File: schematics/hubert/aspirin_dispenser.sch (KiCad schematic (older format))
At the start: 3 parts, among them M6 NEMA 17 Stepper Motor

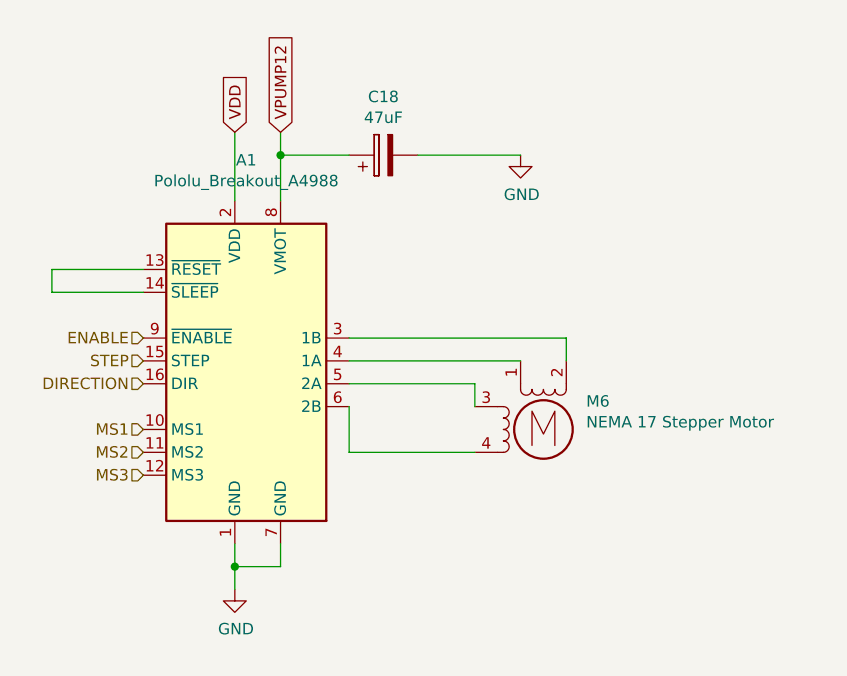
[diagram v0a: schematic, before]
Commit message: updated schematics
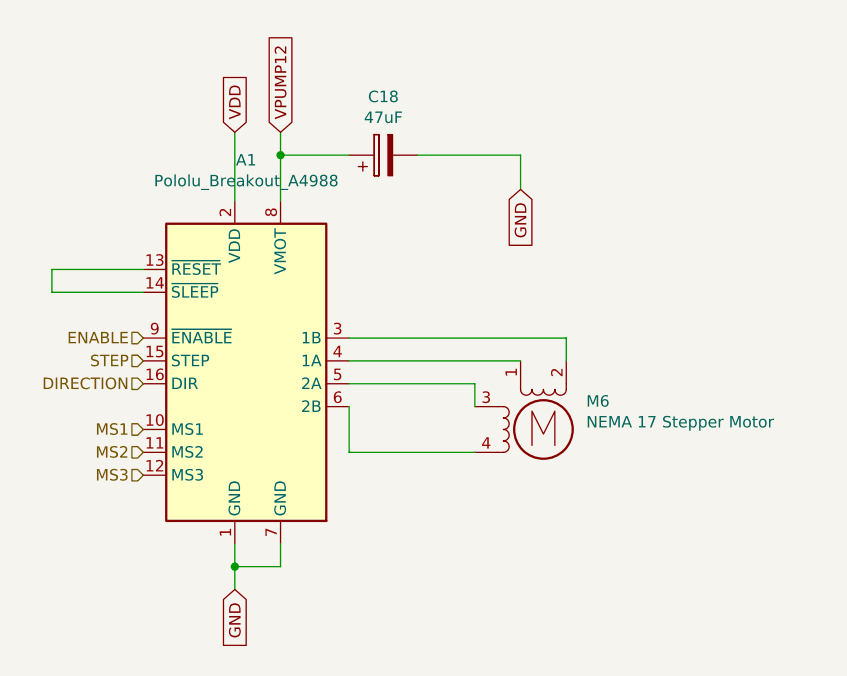
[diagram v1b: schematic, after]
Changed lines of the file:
@@
 $Descr A4 11693 8268
 encoding utf-8
-Sheet 5 6
-Title ""
-Date ""
-Rev ""
+Sheet 5 7
+Title "Hubert"
+Date "2018-11-02"
+Rev "1.1"
 Comp ""
 Comment1 ""
@@
 Wire Wire Line
 	4700 2950 5100 2950
-$Comp
-L power:GND #PWR015
-U 1 1 5BDB44B8
-P 5500 4250
-F 0 "#PWR015" H 5500 4000 50  0001 C CNN
-F 1 "GND" H 5505 4077 50  0000 C CNN
-F 2 "" H 5500 4250 50  0001 C CNN
-F 3 "" H 5500 4250 50  0001 C CNN
-	1    5500 4250
-	1    0    0    -1
-$EndComp
 Wire Wire Line
 	5500 4050 5500 4150
@@
 Wire Wire Line
 	5700 2350 5700 2250
-$Comp
-L power:GND #PWR017
-U 1 1 5BDB595D
-P 6750 2350
-F 0 "#PWR017" H 6750 2100 50  0001 C CNN
-F 1 "GND" H 6755 2177 50  0000 C CNN
-F 2 "" H 6750 2350 50  0001 C CNN
-F 3 "" H 6750 2350 50  0001 C CNN
-	1    6750 2350
-	1    0    0    -1
-$EndComp
 Wire Wire Line
 	6300 2350 6750 2350
@@
 Text GLabel 5700 2250 1    50   Input ~ 0
 VPUMP12
+Text GLabel 5500 4250 3    50   Input ~ 0
+GND
+Text GLabel 6750 2500 3    50   Input ~ 0
+GND
+Wire Wire Line
+	6750 2500 6750 2350
 $EndSCHEMATC

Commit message: fixed ERC problems and added connector for input pins
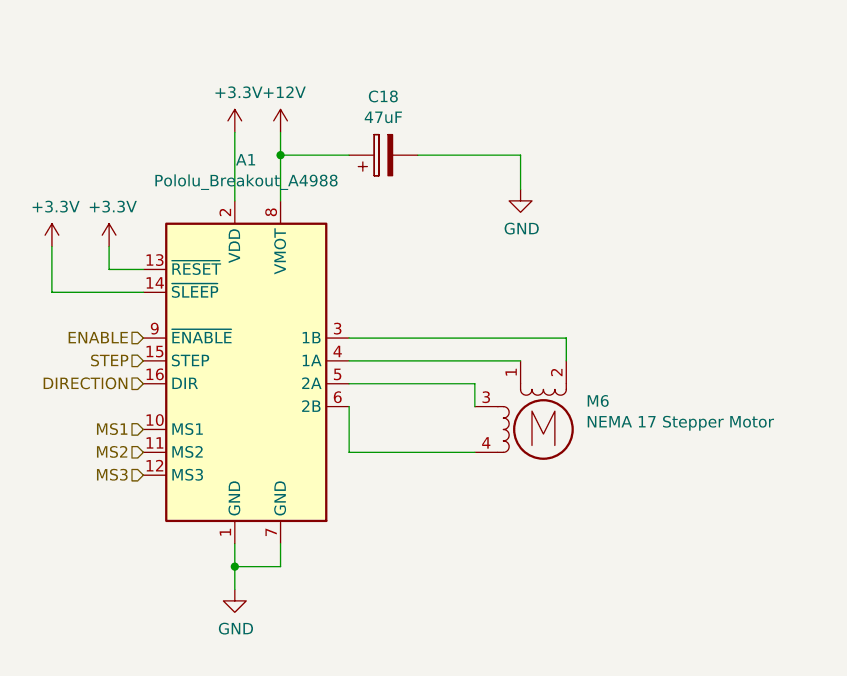
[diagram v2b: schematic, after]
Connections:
- net VDD is gone; now on net +3V3: A1.2 (VDD)
- net +3V3: now reaches A1.13 (~RESET), A1.14 (~SLEEP)
- net VPUMP12 renamed +12V
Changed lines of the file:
@@
 $EndComp
-Wire Wire Line
-	5100 2850 4700 2850
-Wire Wire Line
-	4700 2850 4700 2950
-Wire Wire Line
-	4700 2950 5100 2950
 Wire Wire Line
 	5500 4050 5500 4150
@@
 Wire Wire Line
 	5500 2250 5500 2550
-Text GLabel 5500 2250 1    50   Input ~ 0
-VDD
-Text GLabel 5700 2250 1    50   Input ~ 0
-VPUMP12
-Text GLabel 5500 4250 3    50   Input ~ 0
-GND
-Text GLabel 6750 2500 3    50   Input ~ 0
-GND
 Wire Wire Line
 	6750 2500 6750 2350
+$Comp
+L power:GND #PWR0121
+U 1 1 5BE2C7E5
+P 6750 2500
+F 0 "#PWR0121" H 6750 2250 50  0001 C CNN
+F 1 "GND" H 6755 2327 50  0000 C CNN
+F 2 "" H 6750 2500 50  0001 C CNN
+F 3 "" H 6750 2500 50  0001 C CNN
+	1    6750 2500
+	1    0    0    -1
+$EndComp
+$Comp
+L power:GND #PWR0122
+U 1 1 5BE2C7FD
+P 5500 4250
+F 0 "#PWR0122" H 5500 4000 50  0001 C CNN
+F 1 "GND" H 5505 4077 50  0000 C CNN
+F 2 "" H 5500 4250 50  0001 C CNN
+F 3 "" H 5500 4250 50  0001 C CNN
+	1    5500 4250
+	1    0    0    -1
+$EndComp
+$Comp
+L power:+12V #PWR0123
+U 1 1 5BE2C836
+P 5700 2250
+F 0 "#PWR0123" H 5700 2100 50  0001 C CNN
+F 1 "+12V" H 5715 2423 50  0000 C CNN
+F 2 "" H 5700 2250 50  0001 C CNN
+F 3 "" H 5700 2250 50  0001 C CNN
+	1    5700 2250
+	1    0    0    -1
+$EndComp
+$Comp
+L power:+3.3V #PWR0124
+U 1 1 5BE2C868
+P 5500 2250
+F 0 "#PWR0124" H 5500 2100 50  0001 C CNN
+F 1 "+3.3V" H 5515 2423 50  0000 C CNN
+F 2 "" H 5500 2250 50  0001 C CNN
+F 3 "" H 5500 2250 50  0001 C CNN
+	1    5500 2250
+	1    0    0    -1
+$EndComp
+$Comp
+L power:+3.3V #PWR0130
+U 1 1 5BE2DFCD
+P 4950 2750
+F 0 "#PWR0130" H 4950 2600 50  0001 C CNN
+F 1 "+3.3V" H 4965 2923 50  0000 C CNN
+F 2 "" H 4950 2750 50  0001 C CNN
+F 3 "" H 4950 2750 50  0001 C CNN
+	1    4950 2750
+	1    0    0    -1
+$EndComp
+$Comp
+L power:+3.3V #PWR0131
+U 1 1 5BE2DFDE
+P 4700 2750
+F 0 "#PWR0131" H 4700 2600 50  0001 C CNN
+F 1 "+3.3V" H 4715 2923 50  0000 C CNN
+F 2 "" H 4700 2750 50  0001 C CNN
+F 3 "" H 4700 2750 50  0001 C CNN
+	1    4700 2750
+	1    0    0    -1
+$EndComp
+Wire Wire Line
+	4700 2750 4700 2950
+Wire Wire Line
+	4700 2950 5100 2950
+Wire Wire Line
+	5100 2850 4950 2850
+Wire Wire Line
+	4950 2850 4950 2750
 $EndSCHEMATC

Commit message: started working on layout
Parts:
- C18: footprint (none) -> Capacitor_THT:CP_Radial_D6.3mm_P2.50mm
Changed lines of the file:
@@
 Sheet 5 7
 Title "Hubert"
-Date "2018-11-02"
-Rev "1.1"
+Date "2018-11-05"
+Rev "1.2"
 Comp ""
 Comment1 ""
@@
 F 0 "C18" V 6405 2350 50  0000 C CNN
 F 1 "47uF" V 6314 2350 50  0000 C CNN
-F 2 "" H 6188 2200 50  0001 C CNN
+F 2 "Capacitor_THT:CP_Radial_D6.3mm_P2.50mm" H 6188 2200 50  0001 C CNN
 F 3 "~" H 6150 2350 50  0001 C CNN
 	1    6150 2350
